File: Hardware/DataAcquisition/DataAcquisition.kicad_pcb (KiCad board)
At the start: 2 copper layers, 100 x 100 mm, 92 parts, among them J1 Conn_01x04_Female, J2 Conn_01x04_Female, Q1 Q_NJFET_DGS, Q2 Q_NJFET_DGS, Q3 2N7002, Q4 Q_NJFET_DGS, Q5 Q_NJFET_DGS, Q6 Q_NJFET_DGS, Q7 Q_NJFET_DGS, U1 Opamp_Dual_Generic, U2 TL062, U3 STM32F030K6Tx, U4 LM358, U5 Opamp_Dual_Generic, Y1 20MHz

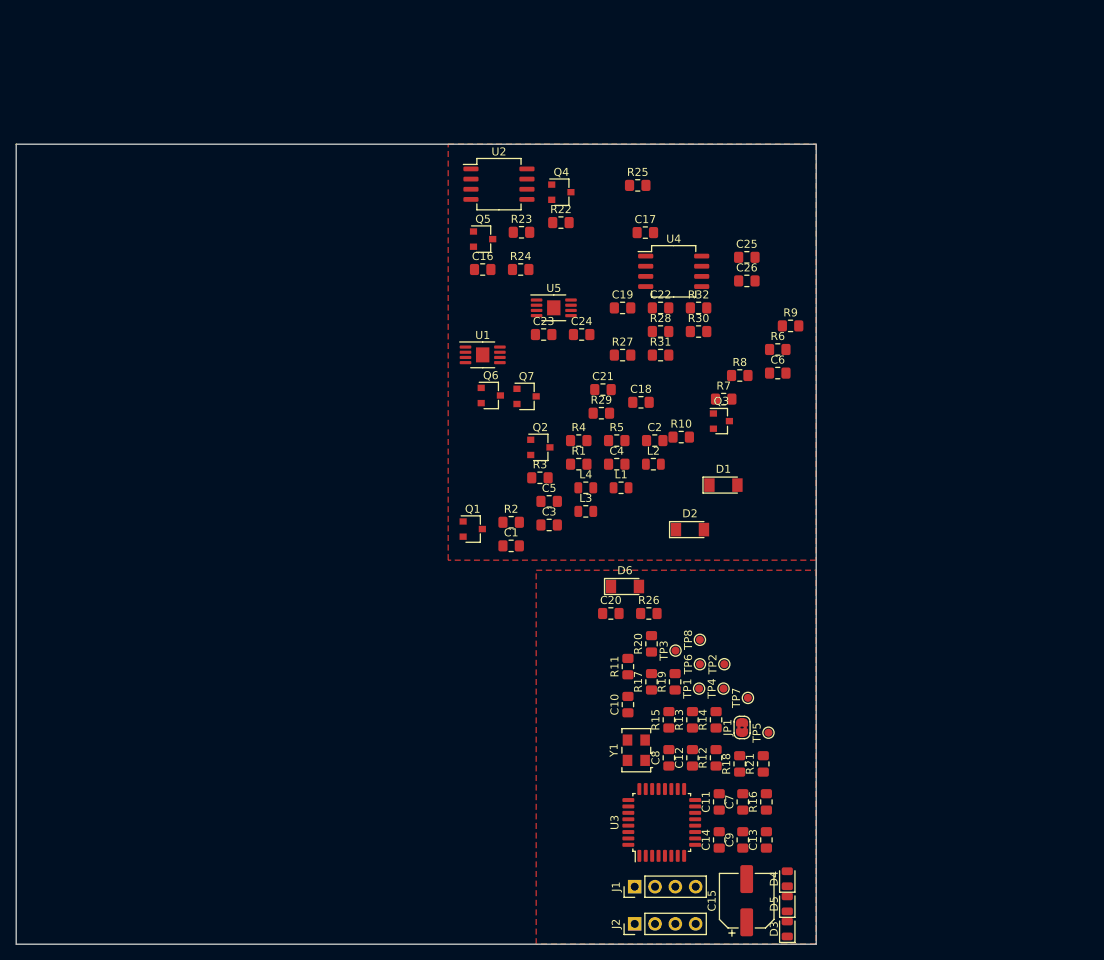
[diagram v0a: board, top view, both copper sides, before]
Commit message: Finished PCB for HV power supply, added correct PCB outlines for acquisition PCB.
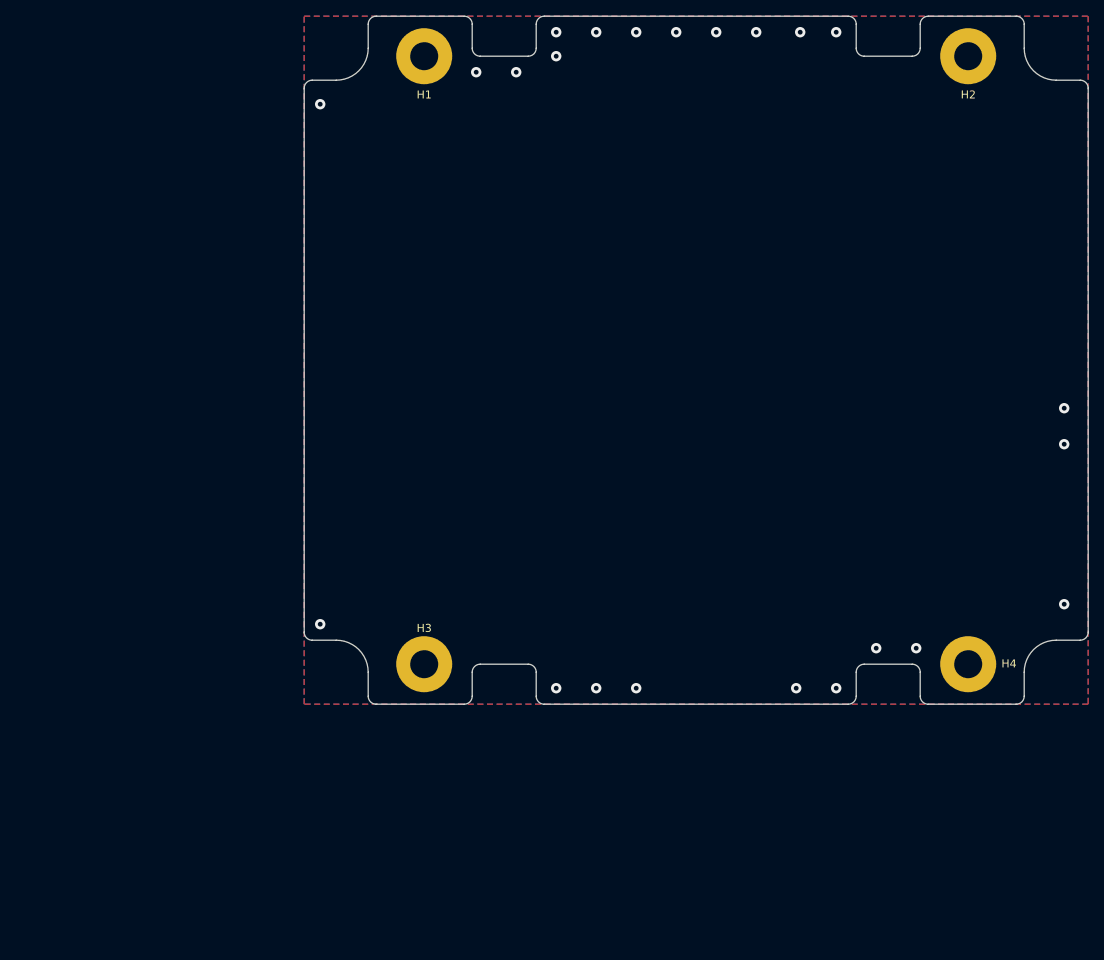
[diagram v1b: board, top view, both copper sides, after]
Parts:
- removed C1, C10, C11, C12, C13, C14, C16, C19, C2, C20, C23, C24, C25, C26, C3, C4, C5, C9: 100n, Capacitor_SMD:C_0805_2012Metric_Pad1.15x1.40mm_HandSolder
- removed C15: 220u, Capacitor_SMD:CP_Elec_6.3x5.8
- removed C17: 47n, Capacitor_SMD:C_0805_2012Metric_Pad1.15x1.40mm_HandSolder
- removed C18: 2p2, Capacitor_SMD:C_0805_2012Metric_Pad1.15x1.40mm_HandSolder
- removed C21: 100p, Capacitor_SMD:C_0805_2012Metric_Pad1.15x1.40mm_HandSolder
- removed C22: 6p, Capacitor_SMD:C_0805_2012Metric_Pad1.15x1.40mm_HandSolder
- removed C6: 10n, Capacitor_SMD:C_0805_2012Metric_Pad1.15x1.40mm_HandSolder
- removed C7, C8: 8p, Capacitor_SMD:C_0805_2012Metric_Pad1.15x1.40mm_HandSolder
- removed D1, D2: 1n148, Diode_SMD:D_MiniMELF
- removed D3, D4, D5: LED, LED_SMD:LED_0805_2012Metric
- removed D6: D, Diode_SMD:D_MiniMELF
- removed J1, J2: Conn_01x04_Female, Connector_PinHeader_2.54mm:PinHeader_1x04_P2.54mm_Vertical
- removed JP1: Jumper_NC_Small, Jumper:SolderJumper-2_P1.3mm_Bridged2Bar_RoundedPad1.0x1.5mm
- removed L1, L2, L3, L4: L, Inductor_SMD:L_0805_2012Metric
- removed Q1, Q2, Q4, Q5, Q6, Q7: Q_NJFET_DGS, Package_TO_SOT_SMD:SC-59
- removed Q3: 2N7002, Package_TO_SOT_SMD:SOT-23
- removed R1, R16, R17, R2, R27, R28, R29, R3, R30, R4, R5, R6, R7, R9: 10k, Resistor_SMD:R_0805_2012Metric_Pad1.15x1.40mm_HandSolder
- removed R10, R25, R31: 1k, Resistor_SMD:R_0805_2012Metric_Pad1.15x1.40mm_HandSolder
- removed R11, R12, R15: 120R, Resistor_SMD:R_0805_2012Metric_Pad1.15x1.40mm_HandSolder
- removed R13, R14: 10R, Resistor_SMD:R_0805_2012Metric_Pad1.15x1.40mm_HandSolder
- removed R18, R19: 220R, Resistor_SMD:R_0805_2012Metric_Pad1.15x1.40mm_HandSolder
- removed R20, R21: 2k2, Resistor_SMD:R_0805_2012Metric_Pad1.15x1.40mm_HandSolder
- removed R22, R23: 47R, Resistor_SMD:R_0805_2012Metric_Pad1.15x1.40mm_HandSolder
- removed R24: 470R, Resistor_SMD:R_0805_2012Metric_Pad1.15x1.40mm_HandSolder
- removed R26: 470k, Resistor_SMD:R_0805_2012Metric_Pad1.15x1.40mm_HandSolder
- removed R32: 1M, Resistor_SMD:R_0805_2012Metric_Pad1.15x1.40mm_HandSolder
- removed R8: 100R, Resistor_SMD:R_0805_2012Metric_Pad1.15x1.40mm_HandSolder
- removed TP1, TP2, TP3, TP4, TP5, TP6, TP7, TP8: TestPoint, TestPoint:TestPoint_Pad_D1.0mm
- removed U1, U5: Opamp_Dual_Generic, Package_SO:MSOP-8-1EP_3x3mm_P0.65mm_EP1.68x1.88mm
- removed U2: TL062, Package_SO:SO-8_5.3x6.2mm_P1.27mm
- removed U3: STM32F030K6Tx, Package_QFP:LQFP-32_7x7mm_P0.8mm
- removed U4: LM358, Package_SO:SO-8_5.3x6.2mm_P1.27mm
- removed Y1: 20MHz, Oscillator:Oscillator_SMD_EuroQuartz_XO53-4Pin_5.0x3.2mm
- added H1: MountingHole_Pad, MountingHole:MountingHole_3.5mm_Pad, F.Cu at (76.0, 79.0)
- added H2: MountingHole_Pad, MountingHole:MountingHole_3.5mm_Pad, F.Cu at (144.0, 79.0)
- added H3: MountingHole_Pad, MountingHole:MountingHole_3.5mm_Pad, F.Cu at (76.0, 155.0)
- added H4: MountingHole_Pad, MountingHole:MountingHole_3.5mm_Pad, F.Cu at (144.0, 155.0)
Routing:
- net GND: vias 0 -> 23
- added copper zone on B.Cu, net GND
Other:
- board size 100 x 100 mm -> 98 x 86 mm
- net class high voltage added: clearance 0.6, trace_width 1, via_dia 0.8, via_drill 0.4

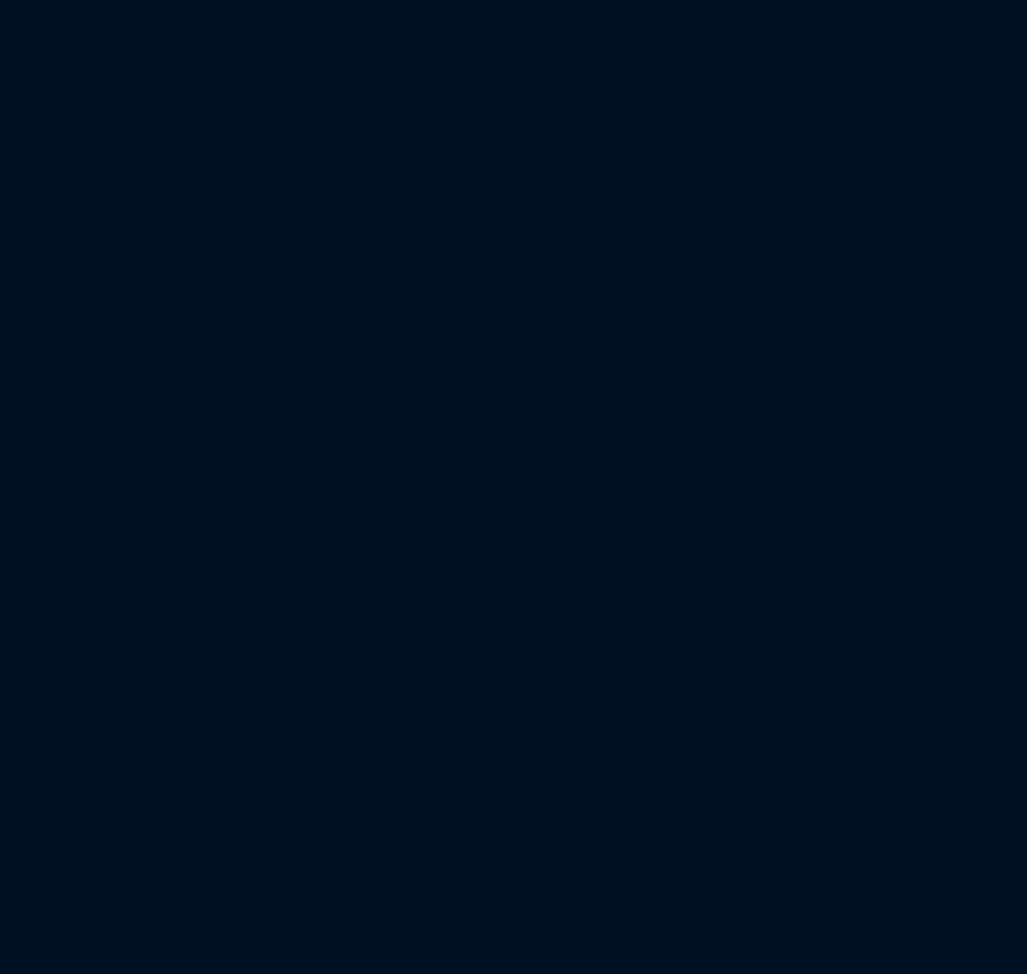
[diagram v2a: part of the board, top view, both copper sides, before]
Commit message: Improve draft of component placement for HV Power Supply, add extra EMI shield.
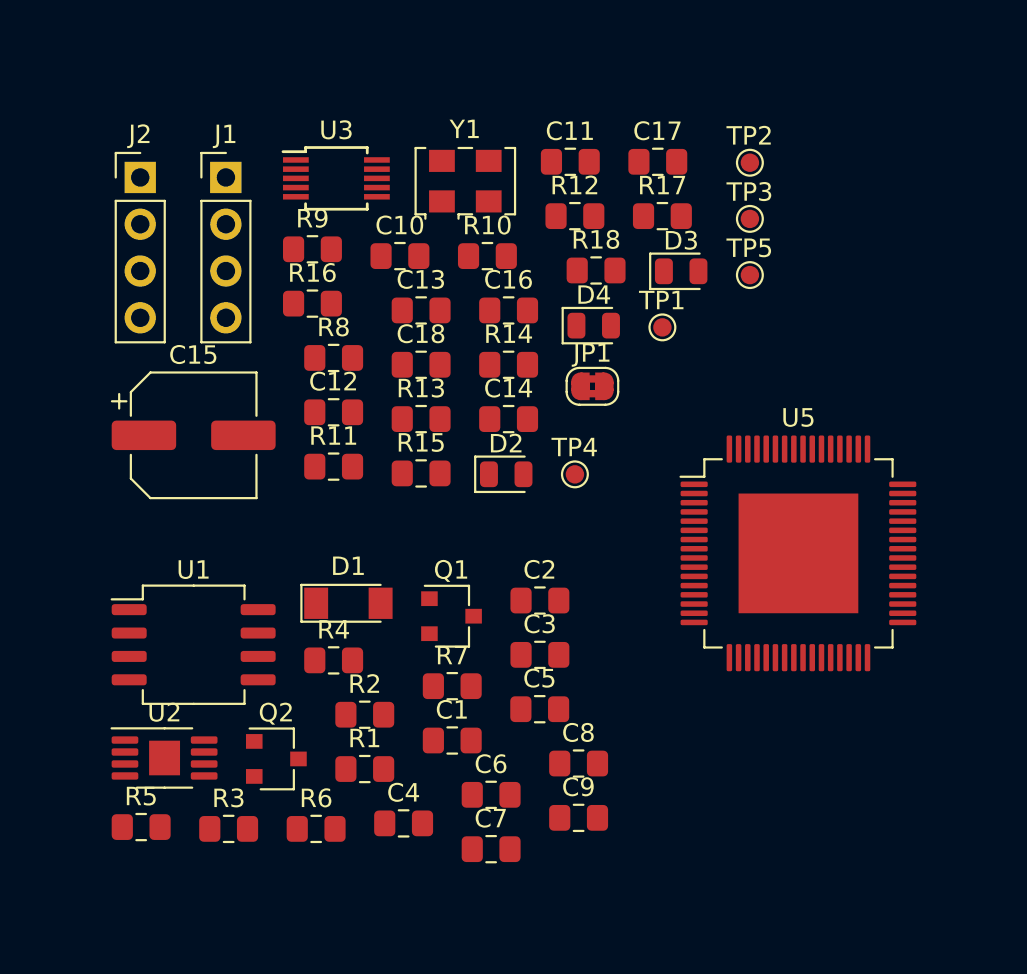
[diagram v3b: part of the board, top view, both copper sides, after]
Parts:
- added C1: 100n, Capacitor_SMD:C_0805_2012Metric_Pad1.15x1.40mm_HandSolder, F.Cu at (105.2, 125.7)
- added C10: 100n, Capacitor_SMD:C_0805_2012Metric_Pad1.15x1.40mm_HandSolder, F.Cu at (102.3, 99.4)
- added C11: 100n, Capacitor_SMD:C_0805_2012Metric_Pad1.15x1.40mm_HandSolder, F.Cu at (111.6, 94.3)
- added C12: 100n, Capacitor_SMD:C_0805_2012Metric_Pad1.15x1.40mm_HandSolder, F.Cu at (98.7, 107.9)
- added C13: 100n, Capacitor_SMD:C_0805_2012Metric_Pad1.15x1.40mm_HandSolder, F.Cu at (103.5, 102.4)
- added C14: 100n, Capacitor_SMD:C_0805_2012Metric_Pad1.15x1.40mm_HandSolder, F.Cu at (108.2, 108.3)
- added C15: 220u, Capacitor_SMD:CP_Elec_6.3x5.8, F.Cu at (91.1, 109.2)
- added C16: 8p, Capacitor_SMD:C_0805_2012Metric_Pad1.15x1.40mm_HandSolder, F.Cu at (108.2, 102.4)
- added C17: 8p, Capacitor_SMD:C_0805_2012Metric_Pad1.15x1.40mm_HandSolder, F.Cu at (116.3, 94.3)
- added C18: 100n, Capacitor_SMD:C_0805_2012Metric_Pad1.15x1.40mm_HandSolder, F.Cu at (103.5, 105.3)
- added C2: 100n, Capacitor_SMD:C_0805_2012Metric_Pad1.15x1.40mm_HandSolder, F.Cu at (109.9, 118.1)
- added C3: 100n, Capacitor_SMD:C_0805_2012Metric_Pad1.15x1.40mm_HandSolder, F.Cu at (109.9, 121.1)
- added C4: 100n, Capacitor_SMD:C_0805_2012Metric_Pad1.15x1.40mm_HandSolder, F.Cu at (102.5, 130.2)
- added C5: 100n, Capacitor_SMD:C_0805_2012Metric_Pad1.15x1.40mm_HandSolder, F.Cu at (109.9, 124.0)
- added C6: 100n, Capacitor_SMD:C_0805_2012Metric_Pad1.15x1.40mm_HandSolder, F.Cu at (107.3, 128.7)
- added C7: 6p, Capacitor_SMD:C_0805_2012Metric_Pad1.15x1.40mm_HandSolder, F.Cu at (107.3, 131.6)
- added C8: 2p2, Capacitor_SMD:C_0805_2012Metric_Pad1.15x1.40mm_HandSolder, F.Cu at (112.0, 127.0)
- added C9: 100p, Capacitor_SMD:C_0805_2012Metric_Pad1.15x1.40mm_HandSolder, F.Cu at (112.0, 129.9)
- added D1: D, Diode_SMD:D_MiniMELF, F.Cu at (99.5, 118.3)
- added D2: LED, LED_SMD:LED_0805_2012Metric, F.Cu at (108.1, 111.3)
- added D3: LED, LED_SMD:LED_0805_2012Metric, F.Cu at (117.6, 100.3)
- added D4: LED, LED_SMD:LED_0805_2012Metric, F.Cu at (112.8, 103.2)
- added J1: Conn_01x04_Female, Connector_PinHeader_2.54mm:PinHeader_1x04_P2.54mm_Vertical, F.Cu at (92.9, 95.2)
- added J2: Conn_01x04_Female, Connector_PinHeader_2.54mm:PinHeader_1x04_P2.54mm_Vertical, F.Cu at (88.2, 95.2)
- added JP1: Jumper_NC_Small, Jumper:SolderJumper-2_P1.3mm_Bridged2Bar_RoundedPad1.0x1.5mm, F.Cu at (112.8, 106.5)
- added Q1: Q_NJFET_DGS, Package_TO_SOT_SMD:SC-59, F.Cu at (105.1, 119.0)
- added Q2: Q_NJFET_DGS, Package_TO_SOT_SMD:SC-59, F.Cu at (95.6, 126.7)
- added R1: 10k, Resistor_SMD:R_0805_2012Metric_Pad1.15x1.40mm_HandSolder, F.Cu at (100.4, 127.3)
- added R10: 2k2, Resistor_SMD:R_0805_2012Metric_Pad1.15x1.40mm_HandSolder, F.Cu at (107.1, 99.4)
- added R11: 120R, Resistor_SMD:R_0805_2012Metric_Pad1.15x1.40mm_HandSolder, F.Cu at (98.7, 110.9)
- added R12: 120R, Resistor_SMD:R_0805_2012Metric_Pad1.15x1.40mm_HandSolder, F.Cu at (111.8, 97.3)
- added R13: 120R, Resistor_SMD:R_0805_2012Metric_Pad1.15x1.40mm_HandSolder, F.Cu at (103.5, 108.3)
- added R14: 10k, Resistor_SMD:R_0805_2012Metric_Pad1.15x1.40mm_HandSolder, F.Cu at (108.2, 105.3)
- added R15: 220R, Resistor_SMD:R_0805_2012Metric_Pad1.15x1.40mm_HandSolder, F.Cu at (103.5, 111.2)
- added R16: 220R, Resistor_SMD:R_0805_2012Metric_Pad1.15x1.40mm_HandSolder, F.Cu at (97.6, 102.0)
- added R17: 10R, Resistor_SMD:R_0805_2012Metric_Pad1.15x1.40mm_HandSolder, F.Cu at (116.6, 97.3)
- added R18: 10R, Resistor_SMD:R_0805_2012Metric_Pad1.15x1.40mm_HandSolder, F.Cu at (113.0, 100.2)
- added R2: 10k, Resistor_SMD:R_0805_2012Metric_Pad1.15x1.40mm_HandSolder, F.Cu at (100.4, 124.3)
- added R3: 470k, Resistor_SMD:R_0805_2012Metric_Pad1.15x1.40mm_HandSolder, F.Cu at (93.0, 130.5)
- added R4: 10k, Resistor_SMD:R_0805_2012Metric_Pad1.15x1.40mm_HandSolder, F.Cu at (98.7, 121.4)
- added R5: 10k, Resistor_SMD:R_0805_2012Metric_Pad1.15x1.40mm_HandSolder, F.Cu at (88.3, 130.4)
- added R6: 1M, Resistor_SMD:R_0805_2012Metric_Pad1.15x1.40mm_HandSolder, F.Cu at (97.8, 130.5)
- added R7: 1k, Resistor_SMD:R_0805_2012Metric_Pad1.15x1.40mm_HandSolder, F.Cu at (105.2, 122.8)
- added R8: 10k, Resistor_SMD:R_0805_2012Metric_Pad1.15x1.40mm_HandSolder, F.Cu at (98.7, 105.0)
- added R9: 2k2, Resistor_SMD:R_0805_2012Metric_Pad1.15x1.40mm_HandSolder, F.Cu at (97.6, 99.1)
- added TP1: TestPoint, TestPoint:TestPoint_Pad_D1.0mm, F.Cu at (116.6, 103.3)
- added TP2: TestPoint, TestPoint:TestPoint_Pad_D1.0mm, F.Cu at (121.3, 94.4)
- added TP3: TestPoint, TestPoint:TestPoint_Pad_D1.0mm, F.Cu at (121.3, 97.4)
- added TP4: TestPoint, TestPoint:TestPoint_Pad_D1.0mm, F.Cu at (111.8, 111.3)
- added TP5: TestPoint, TestPoint:TestPoint_Pad_D1.0mm, F.Cu at (121.3, 100.5)
- added U1: LM358, Package_SO:SO-8_5.3x6.2mm_P1.27mm, F.Cu at (91.1, 120.5)
- added U2: Opamp_Dual_Generic, Package_SO:MSOP-8-1EP_3x3mm_P0.65mm_EP1.68x1.88mm, F.Cu at (89.5, 126.7)
- added U3: MCP33131-10, Package_SO:MSOP-10_3x3mm_P0.5mm, F.Cu at (98.9, 95.2)
- added U5: PIC32MZ0512EFE064, Package_QFP:LQFP-64-1EP_10x10mm_P0.5mm_EP6.5x6.5mm, F.Cu at (124.0, 115.6)
- added Y1: 20MHz, Oscillator:Oscillator_SMD_EuroQuartz_XO53-4Pin_5.0x3.2mm, F.Cu at (105.9, 95.4)
